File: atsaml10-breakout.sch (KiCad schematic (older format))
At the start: 30 parts

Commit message: Layout almost finished, added 2 LEDs, footprints tweaking
Added two LEDs with simple transistor buffers connected to last two
unused pins. They can be used for debugging, as indicators etc.

Replaced C5 and C6 with 0805 parts as 10uF capacitors in 0603 are
expensive.

L1 footprint needs to be replaced as there are no matching 10uH
inductors in 0603 case.
Proposed replacement part: Coilcraft LPS3015-103MRB
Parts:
- added D1: LED0, LED_SMD:LED_0805_2012Metric, symbol Device:LED
- added D2: LED1, LED_SMD:LED_0805_2012Metric, symbol Device:LED
- added Q1, Q2: BC847, Package_TO_SOT_SMD:SOT-23, symbol Device:Q_NPN_BEC
- added R11, R16: 330R, Resistor_SMD:R_0603_1608Metric, symbol Device:R_Small
- added R12, R13: 47k, Resistor_SMD:R_0603_1608Metric, symbol Device:R_Small
- added R14, R15: 100k, Resistor_SMD:R_0603_1608Metric, symbol Device:R_Small
- C1, C10, C11, C2, C3, C4, C7, C8, C9: renamed from C?; footprint (none) -> Capacitor_SMD:C_0603_1608Metric
- C5, C6: renamed from C?; footprint (none) -> Capacitor_SMD:C_0805_2012Metric
- FB1: renamed from FB?; value 50R/20MHz -> BLM18AG221SN1D; footprint (none) -> Inductor_SMD:L_0603_1608Metric
- J1, J2: renamed from J?; footprint (none) -> Connector_PinHeader_2.54mm:PinHeader_1x16_P2.54mm_Vertical
- J3: renamed from J?; footprint (none) -> Connector_PinHeader_1.27mm:PinHeader_2x05_P1.27mm_Vertical_SMD
- L1: renamed from L?; footprint (none) -> Inductor_SMD:L_0603_1608Metric
- R1, R10, R2, R3, R4, R5, R6, R7, R8, R9: renamed from R?; footprint (none) -> Resistor_SMD:R_0603_1608Metric
- SW1: renamed from SW?; footprint (none) -> Button_Switch_SMD:SW_SPST_CK_RS282G05A3
- Y1: renamed from Y?; footprint (none) -> Crystal:Crystal_SMD_EuroQuartz_EQ161-2Pin_3.2x1.5mm
- Y2: renamed from Y?; footprint (none) -> Crystal:Crystal_SMD_EuroQuartz_MJ-4Pin_5.0x3.2mm; symbol Device:Crystal_Small -> Device:Crystal_GND24_Small
- gave numbers to parts that had none: 1
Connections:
- net labels added: LED0, LED1, PA00, PA01
- wire segments 121 -> 174
- no-connect marks 0 -> 2
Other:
- moved on the sheet: C7, J3, R7, R8, SW1

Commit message: Replaced L1's footprint with Coilcraft LPS3015
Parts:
- L1: footprint Inductor_SMD:L_0603_1608Metric -> Elevendroids_Inductor_SMD:L_Coilcraft_LPS3015
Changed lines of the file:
@@
 F 0 "L1" H 5153 2046 50  0000 L CNN
 F 1 "10uH" H 5153 1955 50  0000 L CNN
-F 2 "Inductor_SMD:L_0603_1608Metric" H 5100 2000 50  0001 C CNN
+F 2 "Elevendroids_Inductor_SMD:L_Coilcraft_LPS3015" H 5100 2000 50  0001 C CNN
 F 3 "~" H 5100 2000 50  0001 C CNN
 	1    5100 2000

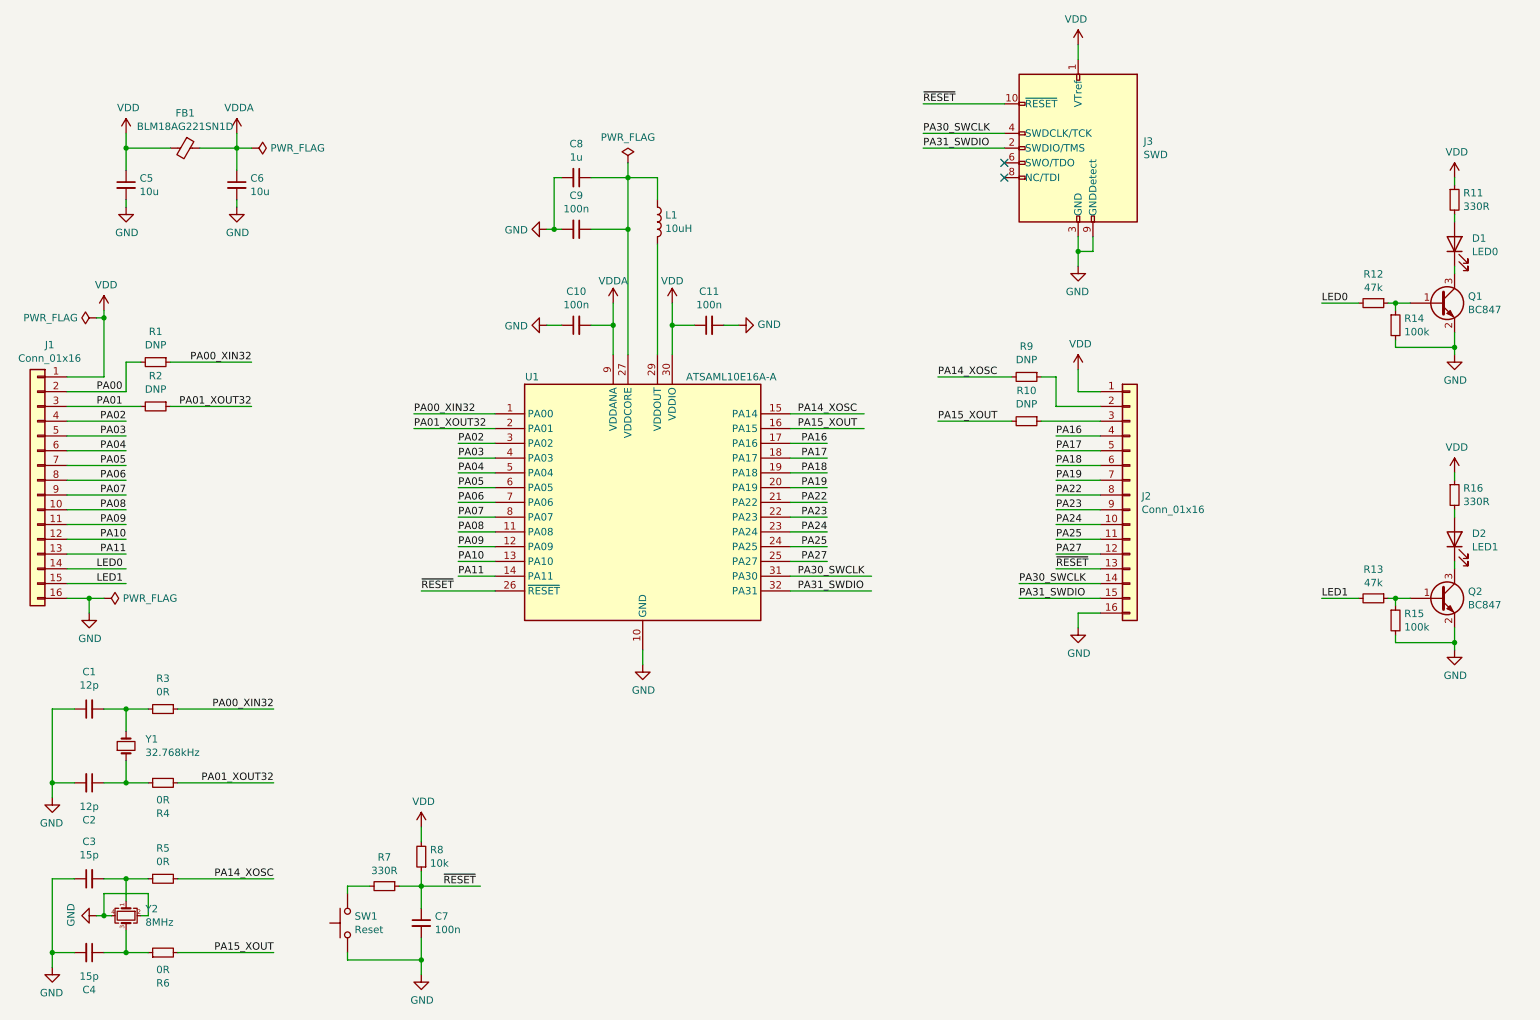
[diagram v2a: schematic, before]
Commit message: Schematic cleanup, more PCB tweaks
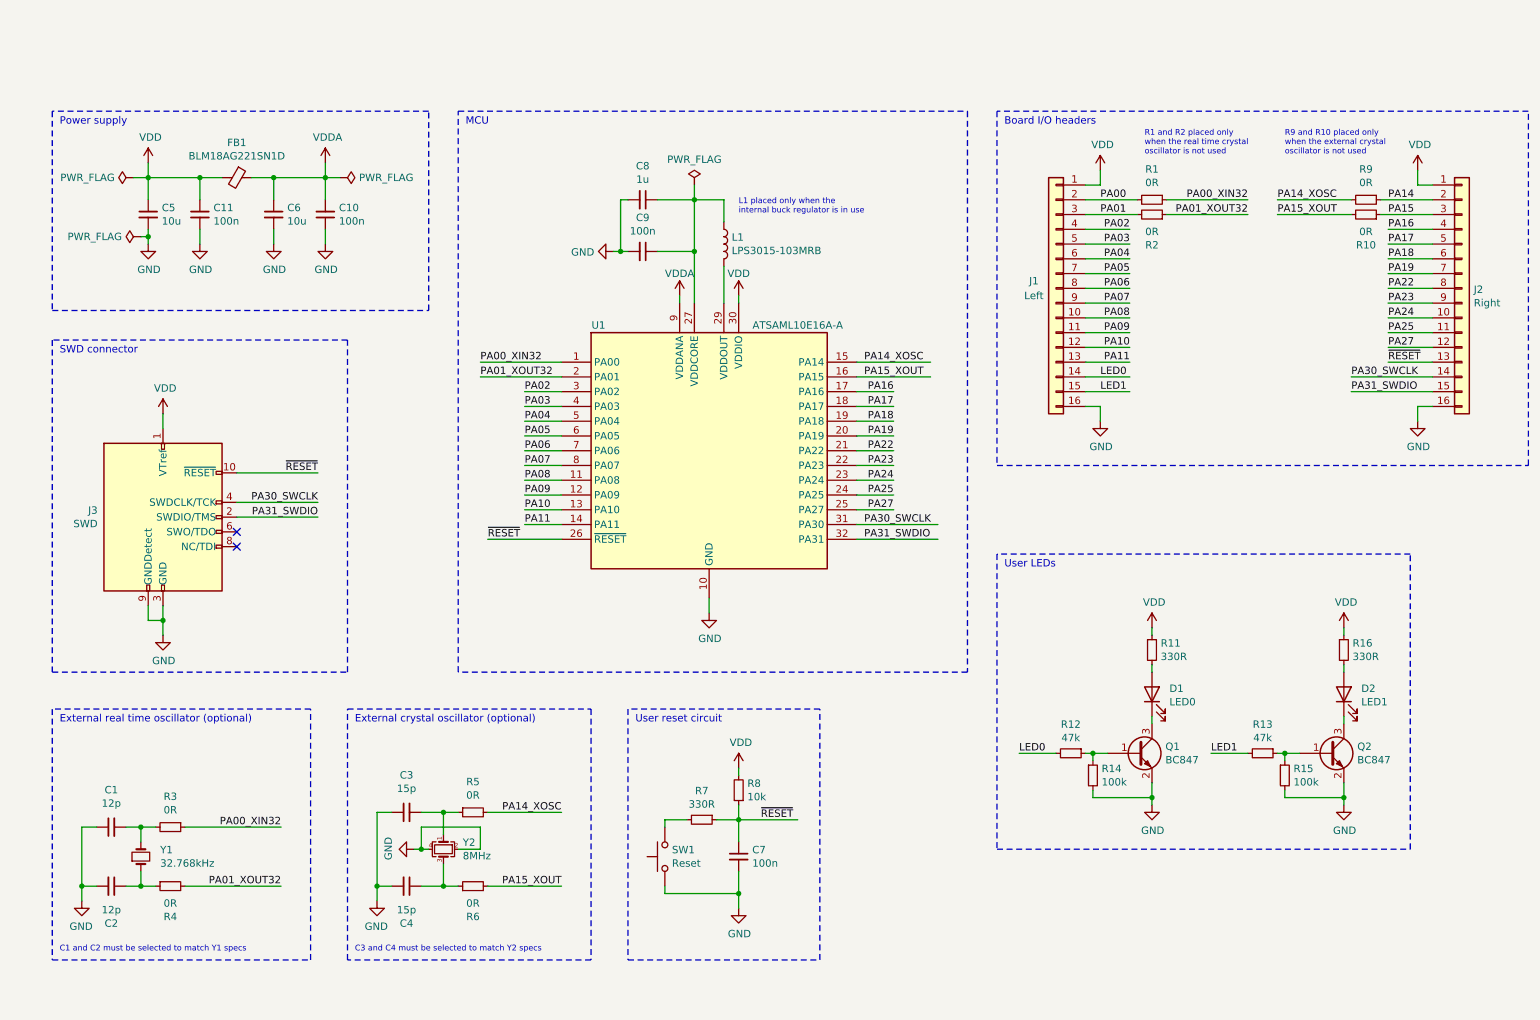
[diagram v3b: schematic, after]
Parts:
- J1: value Conn_01x16 -> Left
- J2: value Conn_01x16 -> Right
- L1: value 10uH -> LPS3015-103MRB
- R1, R10, R2, R9: value DNP -> 0R
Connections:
- net labels added: PA14, PA15
- wire segments 174 -> 170
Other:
- note added: "Board I/O headers"
- note added: "C1 and C2 must be selected to match Y1 specs"
- note added: "C3 and C4 must be selected to match Y2 specs"
- note added: "External crystal oscillator (optional)"
- note added: "External real time oscillator (optional)"
- note added: "L1 placed only when the\ninternal buck regulator is in use"
- note added: "MCU"
- note added: "Power supply"
- note added: "R1 and R2 placed only\nwhen the real time crystal\noscillator is not used"
- note added: "R9 and R10 placed only\nwhen the external crystal\noscillator is not used"
- note added: "SWD connector"
- note added: "User LEDs"
- note added: "User reset circuit"
- moved on the sheet: C1, C10, C11, C2, C3, C4, C5, C6, C7, C8, C9, D1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

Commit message: Getting revision A ready
- Replaced Q1 and Q2 with BC847BDW1 and moved the chip to the front
  layer
- Replaced 0R resistors' packages with 0402
- Filled MFR and MPN fields for some parts
- Added DNP fields for the option jumpers
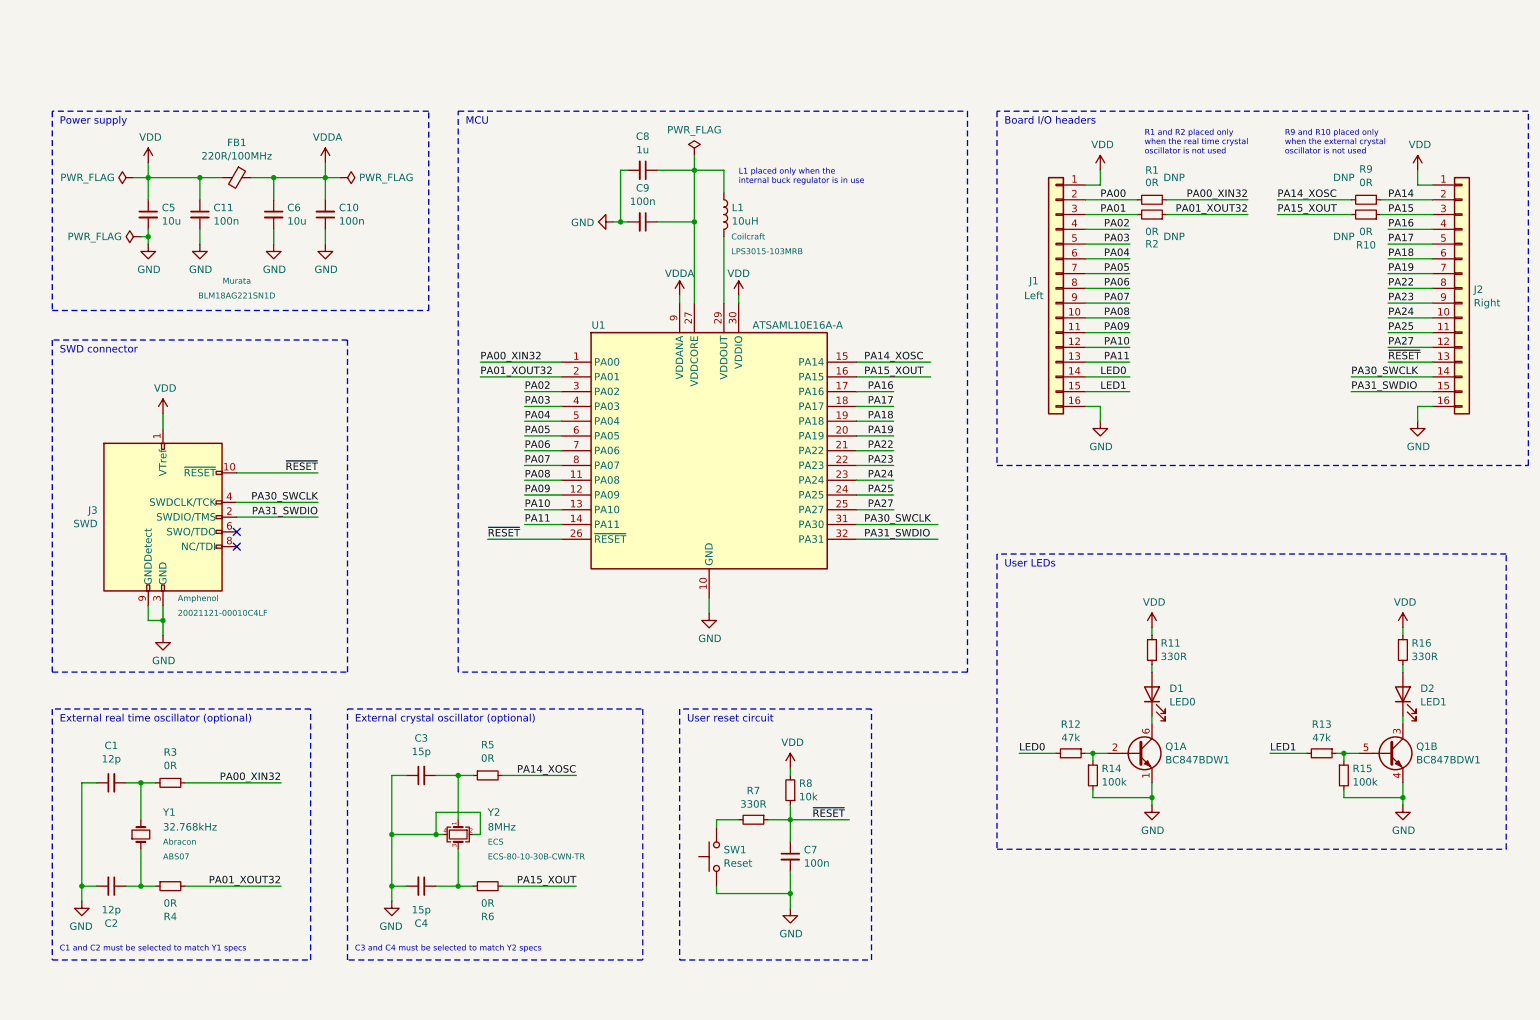
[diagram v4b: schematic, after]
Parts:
- removed Q1, Q2: BC847, Package_TO_SOT_SMD:SOT-23, symbol Device:Q_NPN_BEC
- added Q1: BC847BDW1, Package_TO_SOT_SMD:SOT-363_SC-70-6, symbol Transistor_BJT:BC847BDW1
- FB1: value BLM18AG221SN1D -> 220R/100MHz; MFR (none) -> Murata; MPN (none) -> BLM18AG221SN1D
- J3: MFR (none) -> Amphenol; MPN (none) -> 20021121-00010C4LF
- L1: value LPS3015-103MRB -> 10uH; MFR (none) -> Coilcraft; MPN (none) -> LPS3015-103MRB
- R1, R10, R2, R9: footprint Resistor_SMD:R_0603_1608Metric -> Resistor_SMD:R_0402_1005Metric; DNP (none) -> DNP
- R3, R4, R5, R6: footprint Resistor_SMD:R_0603_1608Metric -> Resistor_SMD:R_0402_1005Metric
- Y1: MFR (none) -> Abracon; MPN (none) -> ABS07
- Y2: MFR (none) -> ECS; MPN (none) -> ECS-80-10-30B-CWN-TR
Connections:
- wire segments 170 -> 171
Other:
- moved on the sheet: C1, C3, C4, C7, C8, C9, D2, L1, R13, R15, R16, R3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

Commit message: Replaced Y2 footprint with a generic one
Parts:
- Y2: footprint Crystal:Crystal_SMD_EuroQuartz_MJ-4Pin_5.0x3.2mm -> Crystal:Crystal_SMD_5032-4Pin_5.0x3.2mm
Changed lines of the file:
@@
 Sheet 1 1
 Title "ATSAML1x Breakout Board"
-Date "2020-09-14"
+Date "2020-09-15"
 Rev "A"
 Comp ""
@@
 F 0 "Y2" V 3600 5950 50  0000 R CNN
 F 1 "8MHz" V 3700 5950 50  0000 R CNN
-F 2 "Crystal:Crystal_SMD_EuroQuartz_MJ-4Pin_5.0x3.2mm" H 3750 6150 50  0001 C CNN
+F 2 "Crystal:Crystal_SMD_5032-4Pin_5.0x3.2mm" H 3750 6150 50  0001 C CNN
 F 3 "https://ecsxtal.com/store/pdf/ecx_53b.pdf" H 3750 6150 50  0001 C CNN
 F 4 "ECS" V 3800 5950 40  0000 R CNN "MFR"

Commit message: Replaced Y1 footprint with a generic one
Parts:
- Y1: footprint Crystal:Crystal_SMD_EuroQuartz_EQ161-2Pin_3.2x1.5mm -> Crystal:Crystal_SMD_3215-2Pin_3.2x1.5mm
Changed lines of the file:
@@
 F 0 "Y1" V 1750 6300 50  0000 L CNN
 F 1 "32.768kHz" V 1650 6300 50  0000 L CNN
-F 2 "Crystal:Crystal_SMD_EuroQuartz_EQ161-2Pin_3.2x1.5mm" H 1600 6150 50  0001 C CNN
+F 2 "Crystal:Crystal_SMD_3215-2Pin_3.2x1.5mm" H 1600 6150 50  0001 C CNN
 F 3 "~" H 1600 6150 50  0001 C CNN
 F 4 "Abracon" V 1550 6300 40  0000 L CNN "MFR"
